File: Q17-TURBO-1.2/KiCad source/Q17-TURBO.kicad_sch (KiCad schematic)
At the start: 93 parts, among them J1 INPUT, J2 SPK+, J3 DC, Q1 IRF610, Q10 KSA992, Q12 KSC1845, Q13 IRF610, Q14 IRF9610, Q15 FQA46N15, Q16 IXTH48P20P, Q17 FQA46N15, Q18 IXTH48P20P, Q2 KSA992, Q3 KSC1845, Q4 IRF9610, Q5 FQPF7P20, Q6 2SK3564, Q7 LSK170B, Q8 DN2540, Q9 BS250P, U1 OPA1611, U2 NDC7003P

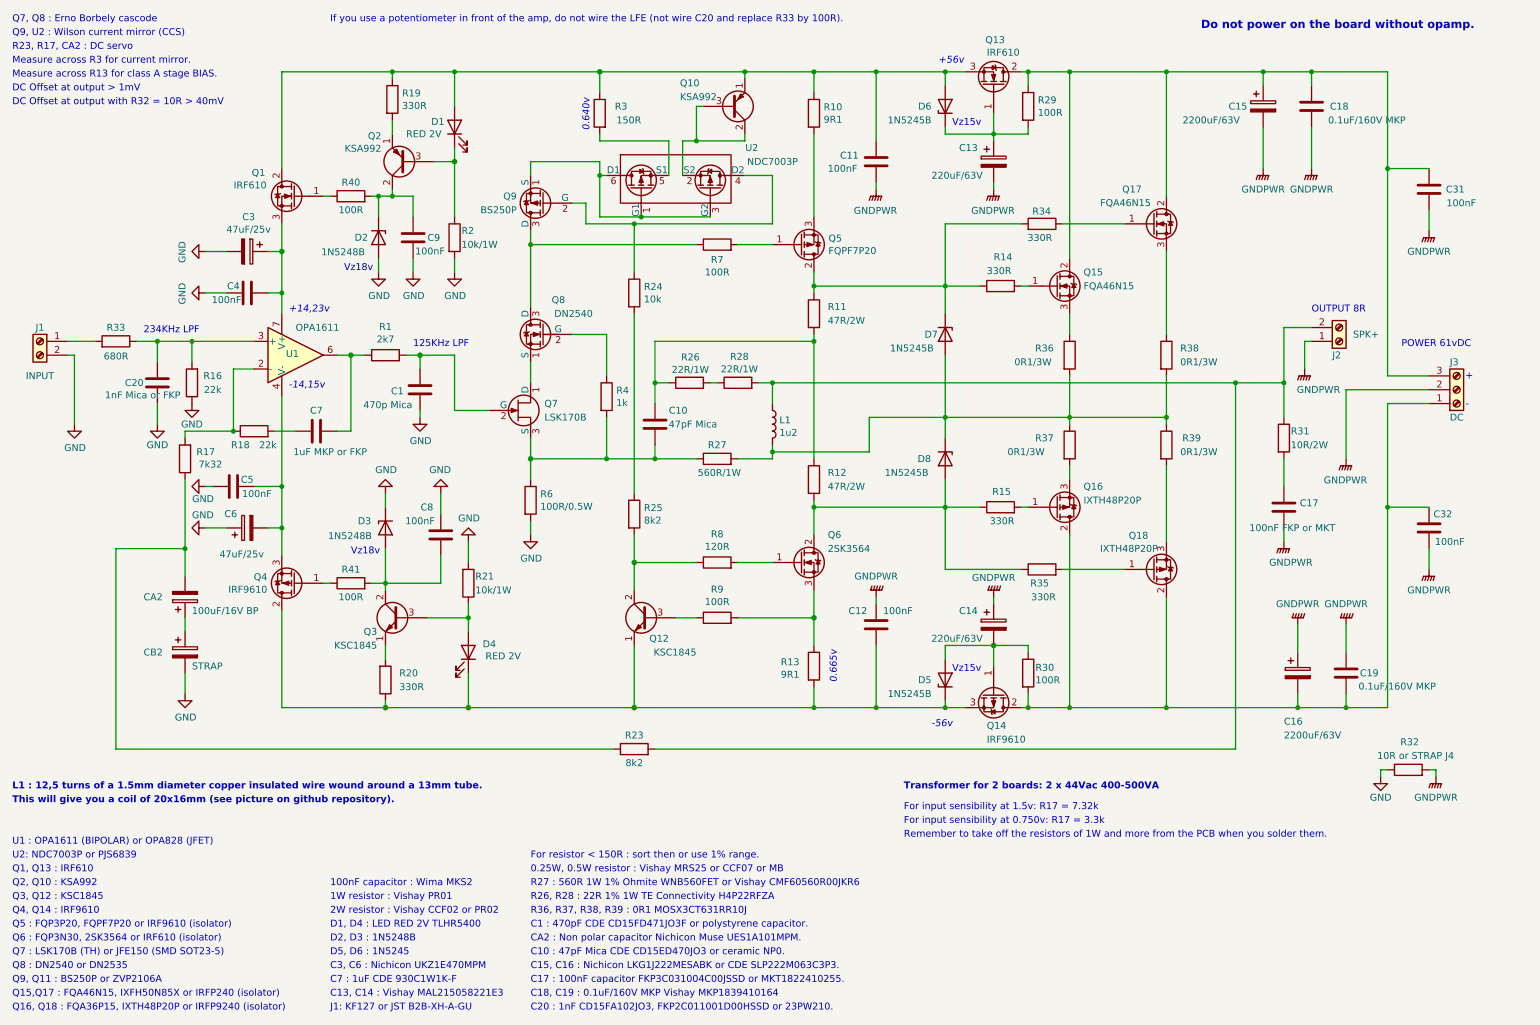
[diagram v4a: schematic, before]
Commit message: Update Q17-Turbo to 1.2.3
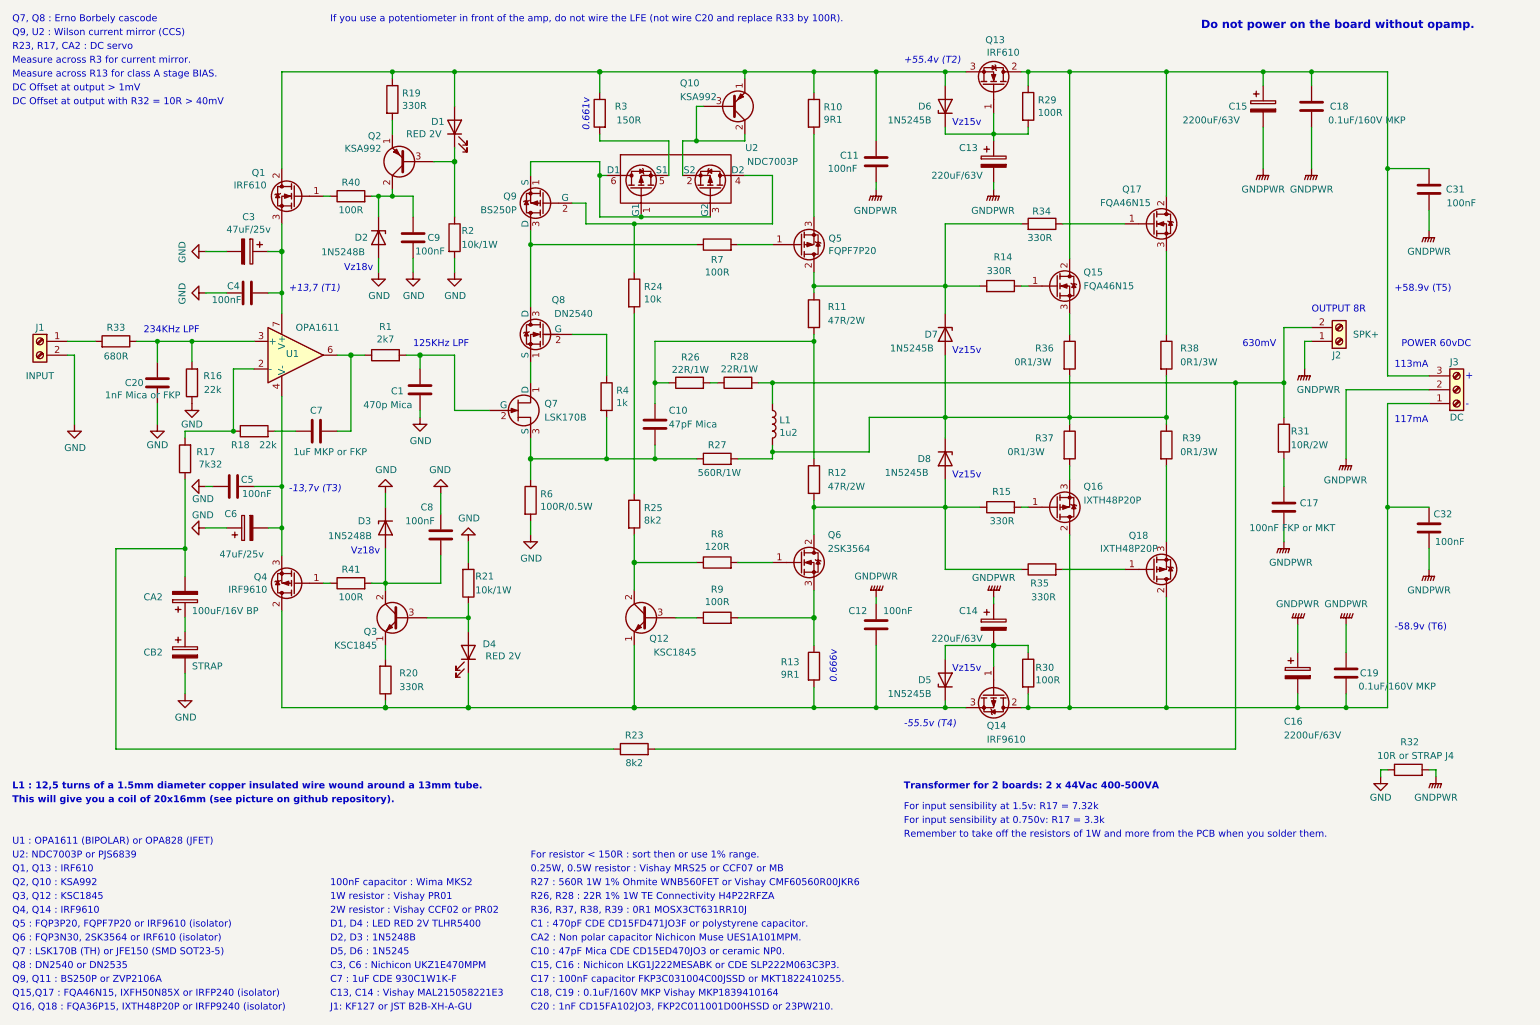
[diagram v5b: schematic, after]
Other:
- note added: "+13,7 (T1)"
- note added: "+55.4v (T2)"
- note added: "+58.9v (T5)"
- note added: "-13,7v (T3)"
- note added: "-55.5v (T4)"
- note added: "-58.9v (T6)"
- note added: "0.661v"
- note added: "0.666v"
- note added: "113mA"
- note added: "117mA"
- note added: "630mV"
- note added: "POWER 60vDC"
- note removed: "+14,23v"
- note removed: "+56v"
- note removed: "-14,15v"
- note removed: "-56v"
- note removed: "0.640v"
- note removed: "0.665v"
- note removed: "POWER 61vDC"
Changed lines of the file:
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@@
   (title_block
     (title "Q17-TURBO (P2) Amplifier")
-    (date "2023-10-12")
-    (rev "1.2.8")
+    (date "2023-10-28")
+    (rev "1.2.9")
     (company "by eng. Tiberiu Vicol")
     (comment 1 "Modified by Stef for the Q17-TURBO project")
@@
     (effects (font (size 1.27 1.27)) (justify left bottom))
   )
-  (text "+14,23v" (at 64.77 68.58 0)
+  (text "-58.9v (T6)" (at 267.97 127 0)
+    (effects (font (size 1.27 1.27)) (justify left bottom))
+  )
+  (text "+13,7 (T1)" (at 64.77 64.77 0)
     (effects (font (size 1.27 1.27) italic) (justify left bottom))
   )
@@
     (effects (font (size 1.27 1.27)) (justify left bottom))
   )
-  (text "+56v" (at 184.15 22.86 0)
+  (text "+55.4v (T2)" (at 177.8 22.86 0)
     (effects (font (size 1.27 1.27) italic) (justify left bottom))
   )
@@
     (effects (font (size 1.27 1.27) (thickness 0.254) bold) (justify left bottom))
   )
+  (text "117mA" (at 267.97 88.9 0)
+    (effects (font (size 1.27 1.27)) (justify left bottom))
+  )
   (text "Vz18v" (at 74.93 60.96 0)
     (effects (font (size 1.27 1.27)) (justify left bottom))
@@
     (effects (font (size 1.27 1.27) (thickness 0.254) bold) (justify left bottom))
   )
+  (text "+58.9v (T5)" (at 267.97 64.77 0)
+    (effects (font (size 1.27 1.27)) (justify left bottom))
+  )
   (text "DC Offset at output > 1mV" (at 13.97 27.94 0)
     (effects (font (size 1.27 1.27)) (justify left bottom))
@@
     (effects (font (size 1.27 1.27)) (justify left bottom))
   )
-  (text "0.640v" (at 120.1615 35.1112 90)
+  (text "0.661v" (at 120.1615 35.1112 90)
     (effects (font (size 1.27 1.27) italic) (justify left bottom))
   )
@@
   )
   (text "234KHz LPF" (at 38.1 72.39 0)
+    (effects (font (size 1.27 1.27)) (justify left bottom))
+  )
+  (text "Vz15v" (at 186.69 99.06 0)
     (effects (font (size 1.27 1.27)) (justify left bottom))
   )
@@
     (effects (font (size 1.27 1.27)) (justify left bottom))
   )
-  (text "-56v" (at 182.88 144.78 0)
+  (text "-55.5v (T4)" (at 177.8 144.78 0)
     (effects (font (size 1.27 1.27) italic) (justify left bottom))
+  )
+  (text "113mA" (at 267.97 78.74 0)
+    (effects (font (size 1.27 1.27)) (justify left bottom))
   )
   (text "Remember to take off the resistors of 1W and more from the PCB when you solder them."
@@
     (effects (font (size 1.27 1.27)) (justify left bottom))
   )
-  (text "0.665v" (at 165.6154 136.5264 90)
+  (text "0.666v" (at 165.6154 136.5264 90)
     (effects (font (size 1.27 1.27) italic) (justify left bottom))
   )
@@
     (effects (font (size 1.27 1.27)) (justify left bottom))
   )
-  (text "POWER 61vDC" (at 269.24 74.93 0)
+  (text "POWER 60vDC" (at 269.24 74.93 0)
     (effects (font (size 1.27 1.27)) (justify left bottom))
   )
@@
     (effects (font (size 1.27 1.27)) (justify left bottom))
   )
+  (text "Vz15v" (at 186.69 76.2 0)
+    (effects (font (size 1.27 1.27)) (justify left bottom))
+  )
   (text "R36, R37, R38, R39 : 0R1 MOSX3CT631RR10J" (at 109.22 179.07 0)
     (effects (font (size 1.27 1.27)) (justify left bottom))
@@
     (effects (font (size 1.27 1.27)) (justify left bottom))
   )
+  (text "630mV" (at 240.03 74.93 0)
+    (effects (font (size 1.27 1.27)) (justify left bottom))
+  )
   (text "Vz15v" (at 186.69 134.62 0)
     (effects (font (size 1.27 1.27)) (justify left bottom))
@@
     (effects (font (size 1.27 1.27)) (justify left bottom))
   )
-  (text "-14,15v" (at 64.77 82.55 0)
+  (text "-13,7v (T3)" (at 64.77 101.6 0)
     (effects (font (size 1.27 1.27) italic) (justify left bottom))
   )

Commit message: Update Q17-Turbo to 1.2.3
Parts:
- C15, C16: Mouser 598-SLP222M063C3P3 -> 647-LKG1J222MESABK; Part# SLP222M063C3P3 -> LKG1J222MESABK
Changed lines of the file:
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@@
   (title_block
     (title "Q17-TURBO (P2) Amplifier")
-    (date "2023-10-28")
+    (date "2023-10-30")
     (rev "1.2.9")
     (company "by eng. Tiberiu Vicol")
@@
       (effects (font (size 1.27 1.27)) hide)
     )
-    (property "Part#" "SLP222M063C3P3" (at 250.19 134.62 0)
-      (effects (font (size 1.27 1.27)) hide)
-    )
-    (property "Mouser" "598-SLP222M063C3P3" (at 250.19 134.62 0)
+    (property "Part#" "LKG1J222MESABK" (at 250.19 134.62 0)
+      (effects (font (size 1.27 1.27)) hide)
+    )
+    (property "Mouser" "647-LKG1J222MESABK" (at 250.19 134.62 0)
       (effects (font (size 1.27 1.27)) hide)
     )
@@
       (effects (font (size 1.27 1.27)) hide)
     )
-    (property "Datasheet" "https://www.mouser.fr/datasheet/2/88/SLP-3081773.pdf" (at 243.84 30.48 0)
-      (effects (font (size 1.27 1.27)) hide)
-    )
-    (property "Part#" "SLP222M063C3P3" (at 243.84 30.48 0)
-      (effects (font (size 1.27 1.27)) hide)
-    )
-    (property "Mouser" "598-SLP222M063C3P3" (at 243.84 30.48 0)
-      (effects (font (size 1.27 1.27)) hide)
-    )
+    (property "Datasheet" "https://www.mouser.fr/datasheet/2/293/e_lkg-3082231.pdf" (at 243.84 30.48 0)
+      (effects (font (size 1.27 1.27)) hide)
+    )
+    (property "Part#" "LKG1J222MESABK" (at 243.84 30.48 0)
+      (effects (font (size 1.27 1.27)) hide)
+    )
+    (property "Mouser" "647-LKG1J222MESABK" (at 243.84 30.48 0)
+      (effects (font (size 1.27 1.27)) hide)
+    )

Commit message: Update Q17-Turbo to 1.2.3
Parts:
- J3: Mouser 651-1755596 -> 571-638491; Part# Terminal Block Phoenix Contact 1755596 -> Terminal 250 FASTON 63849-1 (x3)
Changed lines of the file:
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@@
   (title_block
     (title "Q17-TURBO (P2) Amplifier")
-    (date "2023-10-30")
+    (date "2023-10-31")
     (rev "1.2.9")
     (company "by eng. Tiberiu Vicol")
@@
       (effects (font (size 1.27 1.27)) hide)
     )
-    (property "Datasheet" "https://www.phoenixcontact.com/us/products/1755596/pdf" (at 279.4 82.55 0)
+    (property "Datasheet" "https://www.te.com/commerce/DocumentDelivery/DDEController?Action=srchrtrv&DocNm=63849&DocType=Customer+Drawing&DocLang=English&PartCntxt=63849-1&DocFormat=pdf" (at 279.4 82.55 0)
       (effects (font (size 1.27 1.27)) hide)
     )
-    (property "Part#" "Terminal Block Phoenix Contact 1755596" (at 279.4 82.55 0)
+    (property "Part#" "Terminal 250 FASTON 63849-1 (x3)" (at 279.4 82.55 0)
       (effects (font (size 1.27 1.27)) hide)
     )
-    (property "Mouser" "651-1755596" (at 279.4 82.55 0)
+    (property "Mouser" "571-638491" (at 279.4 82.55 0)
       (effects (font (size 1.27 1.27)) hide)
     )

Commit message: More updates
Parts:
- C20: value 1nF Mica or FKP -> Not used; Mouser 598-CD15FA102JO3 -> (none); Part# CD15FA102JO3 -> (none)
- C7: value 1uF MKP or FKP -> 2.2uF MKP or FKP; Mouser 598-930C1W1K-F -> 75-MKP1839522164; Part# CDE 930C1W1K-F -> MKP1839522164
- R16: value 22k -> 47k; Mouser 594-MRS25000C2202FCT -> 594-MRS25000C4702FRP; Part# MRS25000C2202FCT00 -> MRS25000C4702FRP00
- R33: value 680R -> strap; Mouser 594-MRS25000C6800FCT -> (none); Part# MRS25000C6800FCT00 -> (none)
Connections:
- net at R33.1, U1.3 (+): no longer C20.2, R16.2
- net at J1.1 (Pin_1), R33.2: now also C20.2, R16.2
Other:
- note added: "C7 : 2.2uF Vishay MKP1839522164"
- note added: "For input sensibility at 0.5Vrms: R17 = 3k3"
- note added: "For input sensibility at 1Vrms: R27 = 7k32"
- note added: "Global gain = ((R17+R18)/R17)x((R27+R6)/R6)"
- note added: "Opamp input gain = 1+R18/R17"
- note added: "The value of R25 depends on the input voltage (42v = 2K7, 50v = 7K5, 60v = 8k2)."
- note removed: "234KHz LPF"
- note removed: "C7 : 1uF CDE 930C1W1K-F"
- note removed: "For input sensibility at 0.750v: R17 = 3.3k"
- note removed: "For input sensibility at 1.5v: R17 = 7.32k"
- note removed: "Remember to take off the resistors of 1W and more from the PCB when you solder them."
- moved on the sheet: R33
